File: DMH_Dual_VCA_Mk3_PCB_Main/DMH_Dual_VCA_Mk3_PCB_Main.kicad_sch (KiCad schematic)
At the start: 58 parts, among them J1 TRS_Jack_6.35mm_Sw, J100 IDC_02x05, J11 Conn_01x06, J12 Conn_01x08, J13 Conn_01x06, J14 Conn_01x06, J15 Conn_01x08, J16 Conn_01x06, J18 Conn_02x03_Odd_Even, J19 Conn_02x03_Odd_Even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

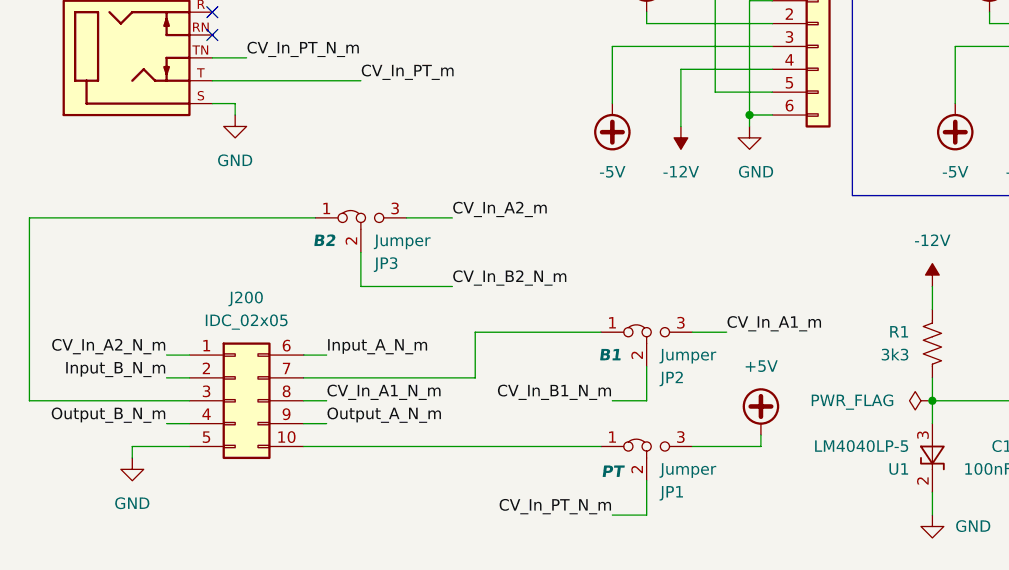
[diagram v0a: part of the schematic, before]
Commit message: Added jumper to normalize Input B to A
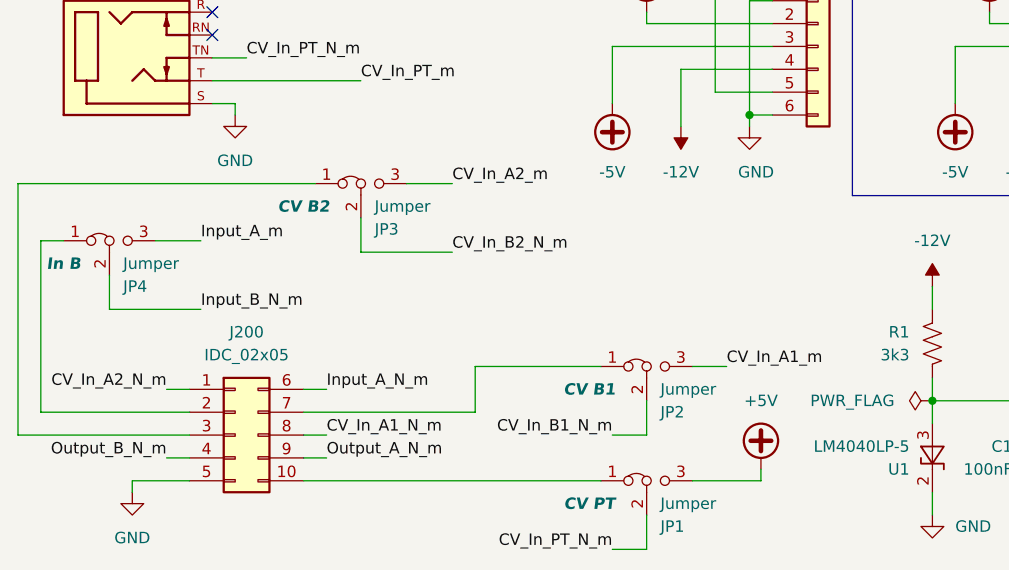
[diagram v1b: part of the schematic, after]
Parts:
- added JP4: Jumper, Connector_PinHeader_2.54mm:PinHeader_1x03_P2.54mm_Vertical, symbol Jumper:Jumper_3_Bridged12
- JP1: Function PT -> CV PT
- JP2: Function B1 -> CV B1
- JP3: Function B2 -> CV B2
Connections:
- net Input_A_m: now also JP4.3 (B)
- net Input_B_N_m: now also JP4.2 (C); no longer J200.2 (Pin_2)
- new net: J200.2 (Pin_2), JP4.1 (A)
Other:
- moved on the sheet: J200, JP1, JP2, JP3

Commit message: Main PCB routing in progress
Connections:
- net Output_A_N_m: now also J200.4 (Pin_4); no longer J200.9 (Pin_9)
- net Output_B_N_m: now also J200.9 (Pin_9); no longer J200.4 (Pin_4)
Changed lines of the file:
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@@
 	)
 	(label "Output_A_N_m"
-		(at 46.99 273.05 0)
-		(effects
-			(font
-				(size 1.27 1.27)
-			)
-			(justify left bottom)
+		(at 29.21 273.05 180)
+		(effects
+			(font
+				(size 1.27 1.27)
+			)
+			(justify right bottom)
 		)
 	)
@@
 	)
 	(label "Output_B_N_m"
-		(at 29.21 273.05 180)
-		(effects
-			(font
-				(size 1.27 1.27)
-			)
-			(justify right bottom)
-		)
-	)
+		(at 46.99 273.05 0)
+		(effects
+			(font
+				(size 1.27 1.27)
+			)
+			(justify left bottom)
+		)
+	)

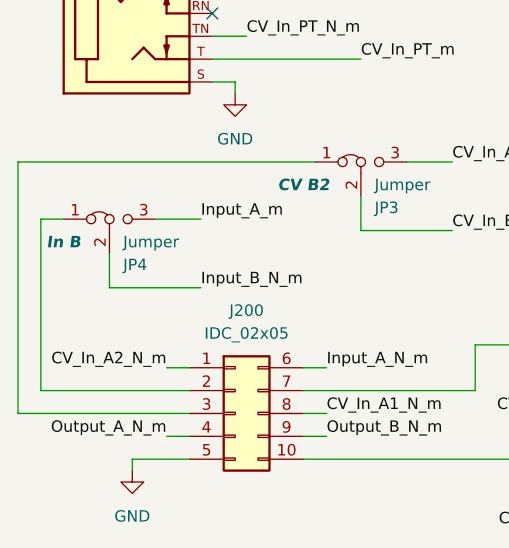
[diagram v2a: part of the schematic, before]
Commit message: Main PCB routing done
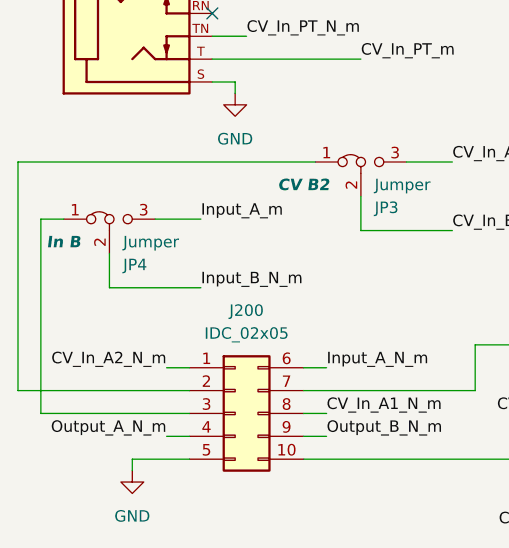
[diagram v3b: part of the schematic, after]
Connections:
- net at JP3.1 (A): now also J200.2 (Pin_2); no longer J200.3 (Pin_3)
- net at JP4.1 (A): now also J200.3 (Pin_3); no longer J200.2 (Pin_2)
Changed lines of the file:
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@@
+	(wire
+		(pts
+			(xy 12.7 267.97) (xy 31.75 267.97)
+		)
+		(stroke
+			(width 0)
+			(type default)
+		)
+	)
 	(wire
 		(pts
@@
 	(wire
 		(pts
+			(xy 15.24 270.51) (xy 31.75 270.51)
+		)
+		(stroke
+			(width 0)
+			(type default)
+		)
+	)
+	(wire
+		(pts
 			(xy 209.55 146.05) (xy 209.55 143.51)
 		)
@@
 	(wire
 		(pts
-			(xy 12.7 270.51) (xy 31.75 270.51)
-		)
-		(stroke
-			(width 0)
-			(type default)
-		)
-	)
-	(wire
-		(pts
 			(xy 45.72 242.57) (xy 12.7 242.57)
 		)
@@
 	(wire
 		(pts
+			(xy 15.24 248.92) (xy 15.24 270.51)
+		)
+		(stroke
+			(width 0)
+			(type default)
+		)
+	)
+	(wire
+		(pts
 			(xy 36.83 31.75) (xy 36.83 30.48)
 		)
@@
 	(wire
 		(pts
-			(xy 12.7 242.57) (xy 12.7 270.51)
+			(xy 12.7 242.57) (xy 12.7 267.97)
 		)
 		(stroke
@@
 	(wire
 		(pts
-			(xy 15.24 248.92) (xy 15.24 267.97)
-		)
-		(stroke
-			(width 0)
-			(type default)
-		)
-	)
-	(wire
-		(pts
 			(xy 198.12 276.86) (xy 198.12 274.32)
 		)
@@
 		)
 		(stroke
-			(width 0)
-			(type default)
-		)
-	)
-	(wire
-		(pts
-			(xy 15.24 267.97) (xy 31.75 267.97)
-		)
-		(stroke
